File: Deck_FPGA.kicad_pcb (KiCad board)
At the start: 4 copper layers, 41 x 30 mm, 72 parts, among them J1 Left side, J2 Right Side, J3 Conn_01x06, U1 XC7A100T-CSG324, U2 TPS65023BRSBT, U3 S25FL128SAGNFI000, U4 LM3880, X1 ASE-100MHz

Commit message: more modifications for jlc
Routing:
- net GND: vias 91 -> 99

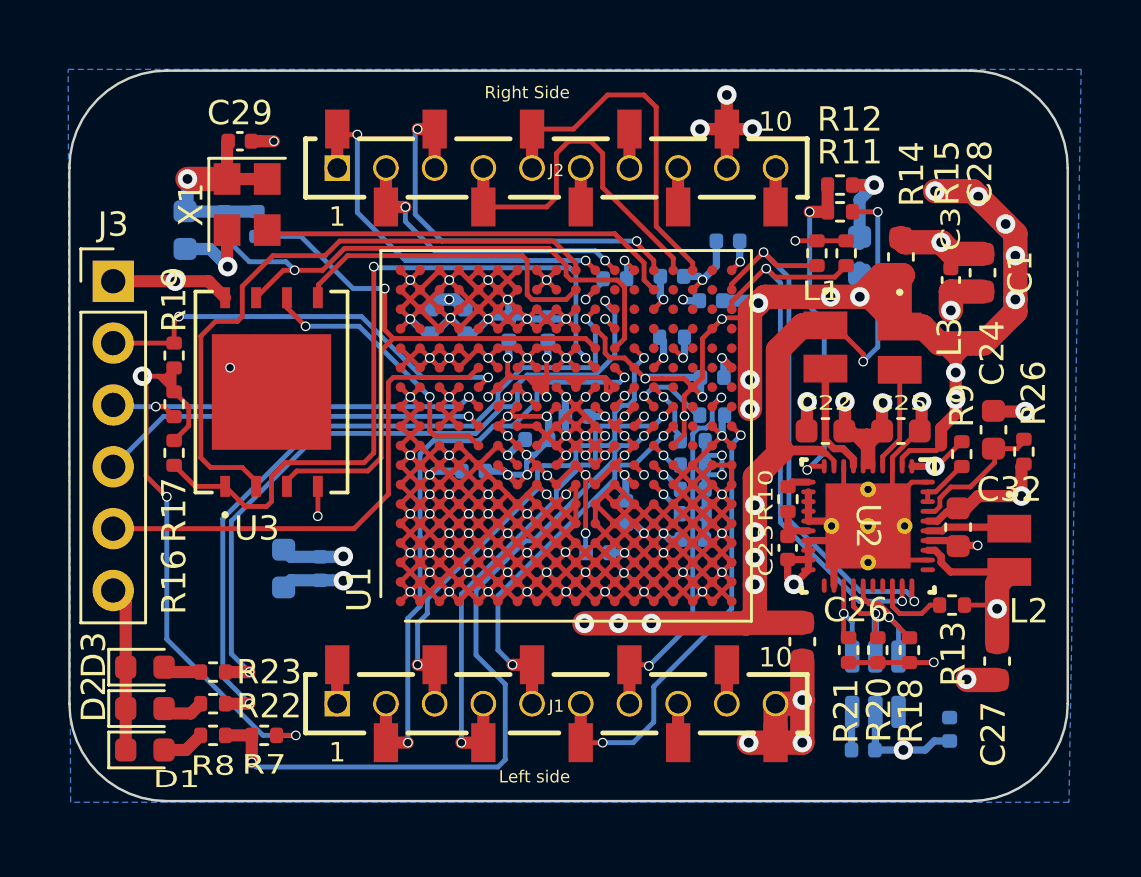
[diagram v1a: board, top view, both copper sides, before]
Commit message: added testpad for program_b and user switch
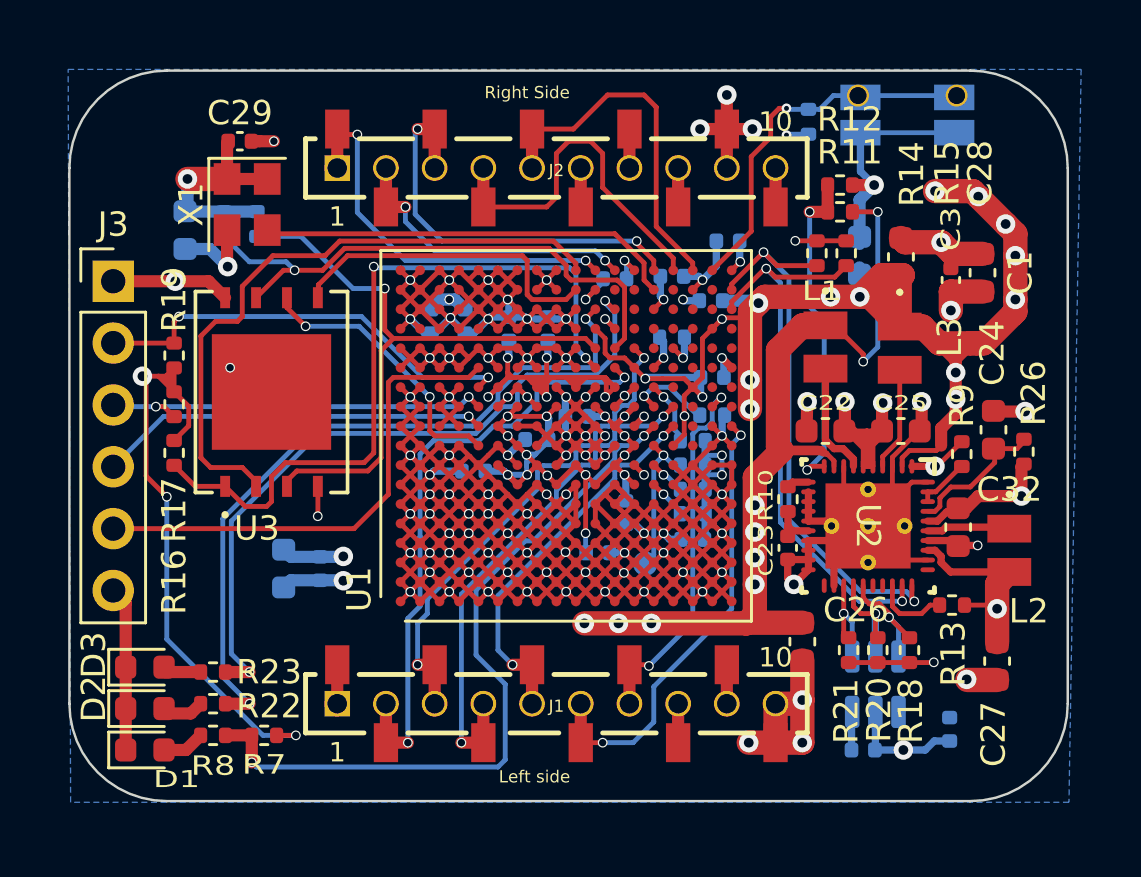
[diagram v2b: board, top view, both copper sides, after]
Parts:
- added R27: 4k7, Resistor_SMD:R_0402_1005Metric, B.Cu at (110.3, 98.1)
- added SW1: Push Button, power_ic:SW_EVQ-P3401P, B.Cu at (114.4, 97.8)
- added TP1: ProgramB_Pad, TestPoint:TestPoint_Pad_D1.0mm, B.Cu at (103.7, 116.2)
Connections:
- U1 pad U18: unconnected-(U1-PadU18) -> /PUSH_BUTTON
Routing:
- net /PUSH_BUTTON: track 0.00 -> 15.3 mm, vias 0 -> 1
- net GND: track 439.3 -> 445.6 mm
- net /PROGRAM_B: track 1.52 -> 6.28 mm
- net +3V3: track 113.9 -> 114.8 mm, vias 28 -> 29

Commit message: final modifications, ordered!
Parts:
- R27, SW1: moved to F.Cu
- moved R27 0.95 mm to (110.0, 97.2), turned to 0 degrees
- turned SW1 to 180 degrees
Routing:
- net +3V3: track 114.8 -> 112.1 mm, vias 29 -> 28
- net GND: track 445.6 -> 444.2 mm, vias 99 -> 100
- net /PUSH_BUTTON: track 15.3 -> 14.8 mm, vias 1 -> 0

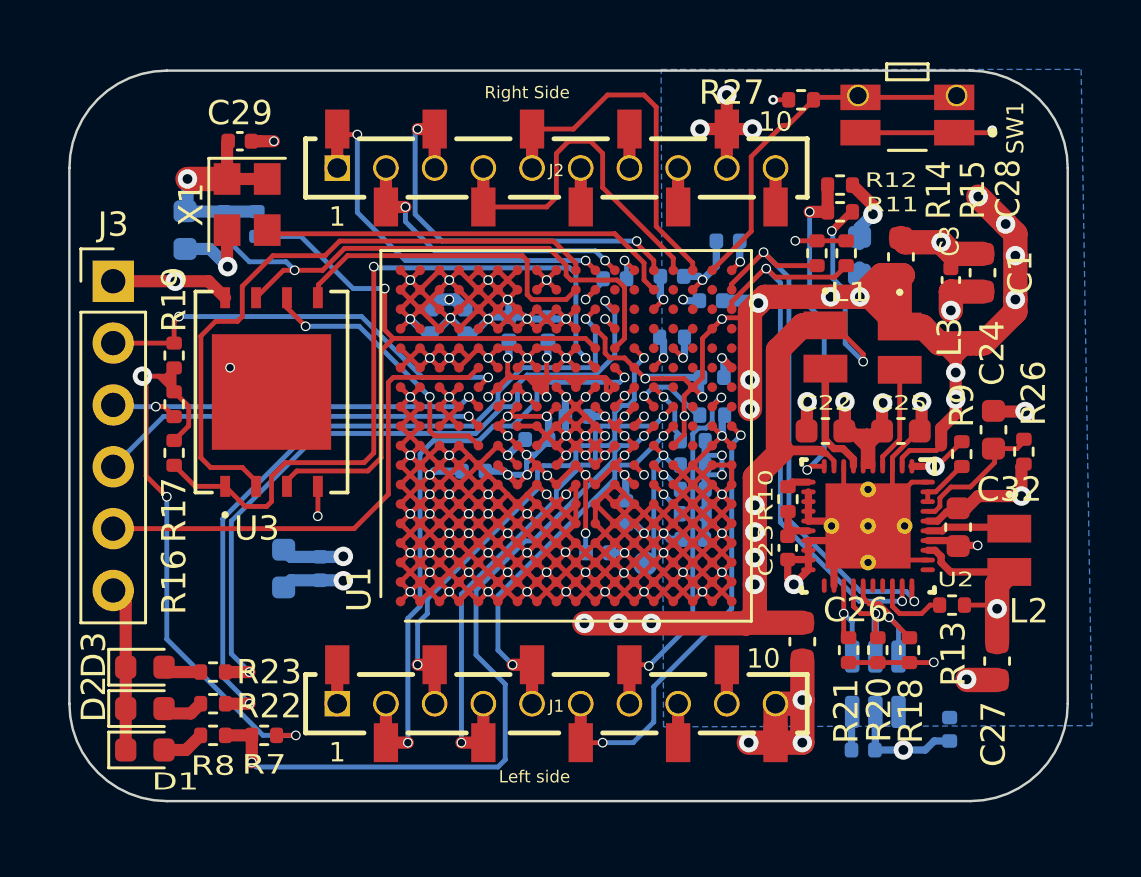
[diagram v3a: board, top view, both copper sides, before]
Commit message: fixed issues after correct setup of DRC
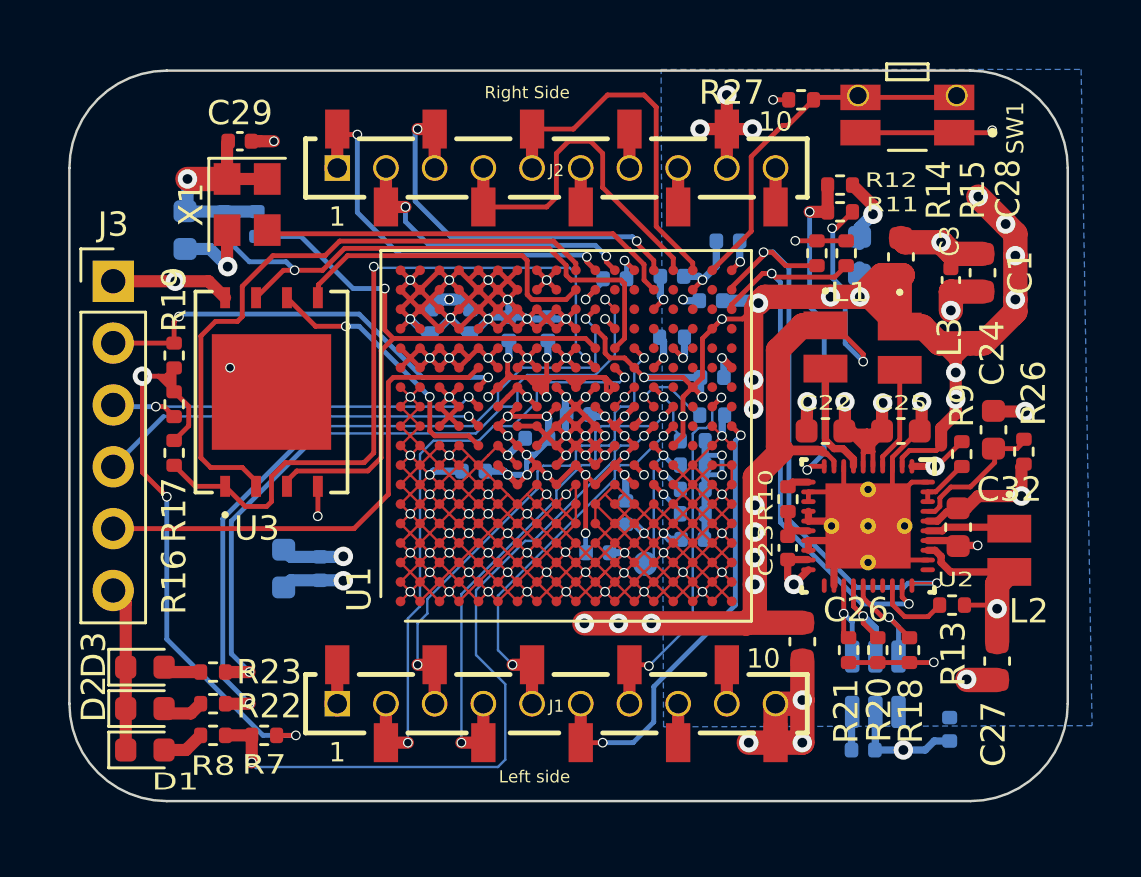
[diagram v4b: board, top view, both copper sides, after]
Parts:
- moved C21 0.22 mm to (96.5, 106.3)
- moved C18 0.09 mm to (100.9, 110.1)
- moved C4 0.05 mm to (99.2, 111.1)
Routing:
- net +1V8: track 80.0 -> 27.2 mm
- net GND: track 444.2 -> 440.9 mm, vias 100 -> 99
- net VBUS: track 30.7 -> 28.6 mm
- net /SCLK_PWR: track 23.2 -> 24.5 mm
- added copper zone on In2.Cu, net +1V8
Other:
- board text removed: "dec1v0"
- board text removed: "dec3v3_0"
